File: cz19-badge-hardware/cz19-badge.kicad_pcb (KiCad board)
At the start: 4 copper layers, 391.4 x 293.4 mm, 323 parts, among them J1 USB_B_Micro, J3 Hook1, J4 Hook2, Q1 AO3400 (A09T), Q2 AO3400 (A09T), Q3 AO3400 (A09T), Q4 AO3400 (A09T), Q5 AO3400 (A09T), Q6 AO3400 (A09T), SW1 SW_Push, SW2 SW_Push, SW3 SW_Push, SW4 SW_Push, SW5 SW_Push, SW6 SW_Push, U1 SM16106, U10 XC6206P332PR, U11 ESP32-WROOM-32D, U2 SM16106, U3 SM16106, U4 SM16106, U5 SM16106, U6 SM16106, U7 TC7258E, U8 CH340C, U9 TP4056

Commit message: Finished PCB in 6mm pixel pitch (no SAO yet)
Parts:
- moved R14 308.0 mm to (25.0, -108.7)
- moved D257 304.0 mm to (38.1, -150.5)
- moved D258 304.0 mm to (40.6, -150.5)
- moved R10 304.0 mm to (42.1, -150.5)
- moved R9 304.0 mm to (36.6, -150.5)
- moved D260 294.1 mm to (42.1, -113.4)
- moved R13 294.1 mm to (43.6, -113.4)
- moved Q3 289.9 mm to (57.3, -112.1)
- moved R11 289.9 mm to (51.9, -112.1)
- moved R24 289.9 mm to (53.4, -112.1)
- moved D259 289.8 mm to (46.9, -113.4)
- moved R12 289.8 mm to (48.4, -113.4)
- moved R16 284.6 mm to (45.4, -135.1), turned to 270 degrees
- moved C1 283.5 mm to (73.8, -149.7)
- moved R15 282.9 mm to (72.3, -149.7)
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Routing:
- net GND: track 12.1 -> 295.6 mm, vias 0 -> 32
- net HUB75_OE: track 0.00 -> 261.4 mm, vias 0 -> 10
- net CLK: track 0.00 -> 248.5 mm, vias 0 -> 9
- net HUB75_LAT: track 0.00 -> 234.4 mm, vias 0 -> 9
- net G0: track 0.00 -> 180.1 mm, vias 0 -> 4
- net HUB75_R0: track 0.00 -> 179.5 mm, vias 0 -> 2
- net C: track 0.01 -> 179.2 mm, vias 0 -> 2
- net A: track 0.00 -> 170.7 mm
- net B: track 0.00 -> 170.6 mm
- net VUSB_SENSE: track 0.00 -> 167.6 mm, vias 0 -> 2
- net BTN_B: track 0.59 -> 166.1 mm, vias 0 -> 2
- net SCL: track 0.00 -> 159.7 mm
- net (no net): track 158.1 -> 0.00 mm, vias 32 -> 0
- net SDA: track 0.00 -> 154.7 mm
- net B0: track 0.00 -> 153.0 mm, vias 0 -> 2
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- added copper zone on 3V3.Cu, net 3V3
- added copper zone on B.Cu, net GND
- added copper zone on VCC.Cu, net VCC
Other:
- board size 391.4 x 293.4 mm -> 192 x 48 mm
- net class Power: trace_width 0.5 -> 0.3
- board text added: "CZ19 1337 badge proto v0.1 aka “Anakin”"
- board text removed: "CZ19 1337 badge proto v0.1 aka “Harry Potter”"
- board text removed: "Spoke width: 0.8mm"
- board text removed: "Spoke width: 1.2mm"

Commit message: Swapped left and right button
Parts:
- moved R23 232.1 mm to (184.3, 72.6), turned to 270 degrees
- moved R20 232.1 mm to (187.3, 72.6), turned to 270 degrees
- moved R21 230.4 mm to (185.8, 72.6), turned to 270 degrees
- moved SW4 228.4 mm to (75.3, 92.4)
- moved BT1 225.3 mm to (169.6, 106.1)
- moved C3 225.3 mm to (92.9, 102.2)
- moved C4 225.3 mm to (138.6, 90.0)
- moved D1 225.3 mm to (56.6, 72.3)
- moved D10 225.3 mm to (110.6, 72.3)
- moved D100 225.3 mm to (74.6, 90.3)
- moved D101 225.3 mm to (80.6, 90.3)
- moved D102 225.3 mm to (86.6, 90.3)
- moved D103 225.3 mm to (92.6, 90.3)
- moved D104 225.3 mm to (98.6, 90.3)
- moved D105 225.3 mm to (104.6, 90.3)
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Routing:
- net -BATT: track 38.4 -> 109.0 mm, vias 6 -> 0
- net Net-(Q4-Pad1): track 0.00 -> 24.4 mm
- net BTN_UP: track 36.1 -> 48.7 mm, vias 2 -> 4
- net BTN_RIGHT: track 51.4 -> 62.7 mm, vias 2 -> 4
- net 3V3: track 24.1 -> 33.9 mm, vias 6 -> 9
- net SCL: track 159.7 -> 167.2 mm, vias 0 -> 2
- net BTN_DOWN: track 60.5 -> 67.3 mm
- net SDA: track 154.7 -> 161.4 mm, vias 0 -> 2
- net G0: track 180.1 -> 186.4 mm, vias 4 -> 6
- net VCC: track 103.0 -> 106.2 mm
- net GND: track 295.6 -> 293.1 mm
- net B1: track 108.2 -> 110.0 mm, vias 2 -> 4
- net Net-(D33-Pad4): track 230.3 -> 231.6 mm
- net Net-(D65-Pad4): track 216.5 -> 217.3 mm
- net G1: track 106.6 -> 107.1 mm, vias 2 -> 4
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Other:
- net class Power: trace_width 0.3 -> 0.5
- board text added: "CZ19 1337 badge proto v0.2 aka “Forrest”"
- board text removed: "CZ19 1337 badge proto v0.1 aka “Anakin”"
- board text removed: "Spoke width: 0.508mm"

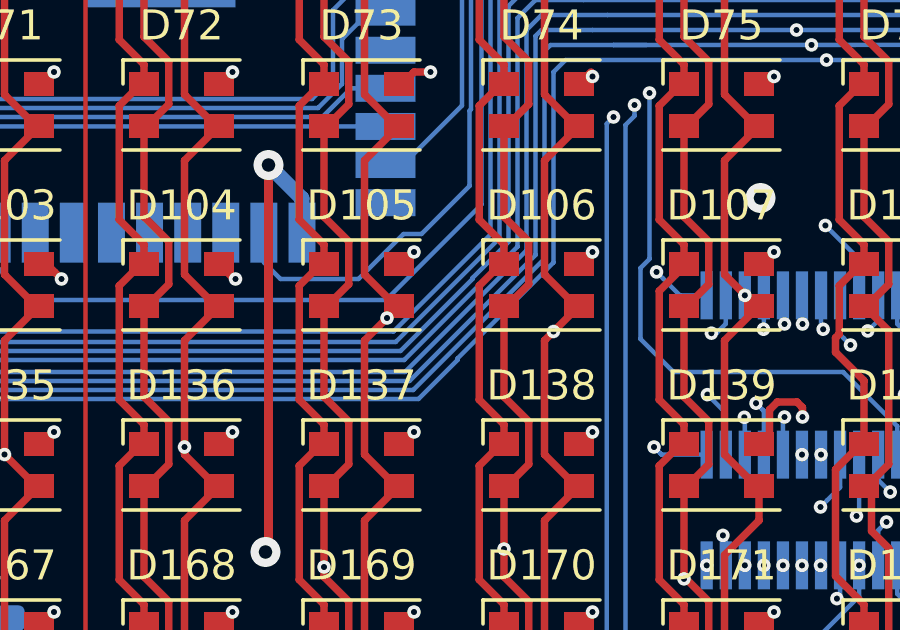
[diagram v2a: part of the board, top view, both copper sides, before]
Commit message: Added pulldown for GPIO12 to prevent boot instability due to flash voltage (seen through EMR)
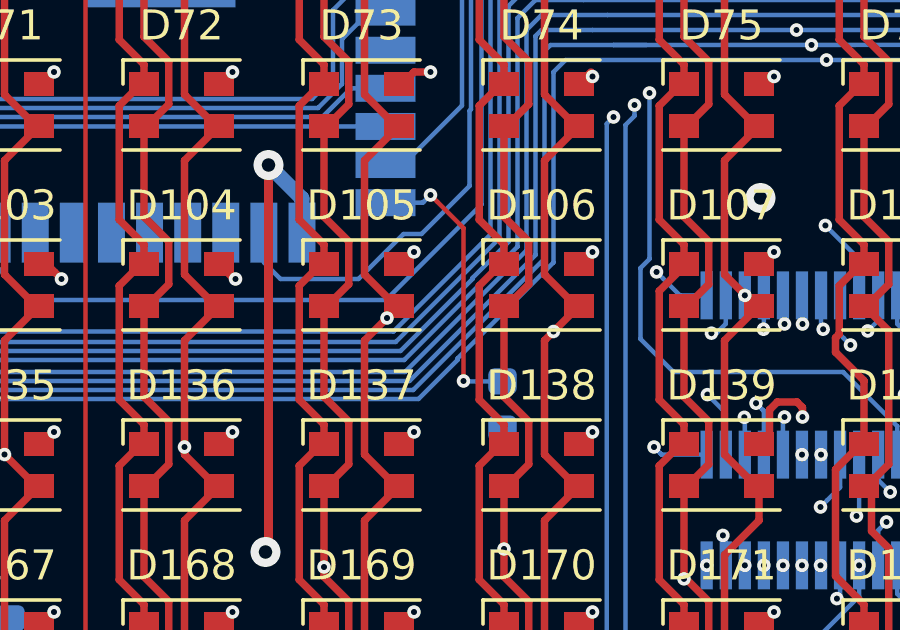
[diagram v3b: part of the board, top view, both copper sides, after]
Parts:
- added R33: 10k, Resistor_SMD:R_0603_1608Metric, B.Cu at (109.3, 94.3)
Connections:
- U11 pad 14: (no net) -> Net-(R33-Pad2)
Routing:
- net Net-(R33-Pad2): track 0.00 -> 9.57 mm, vias 0 -> 2

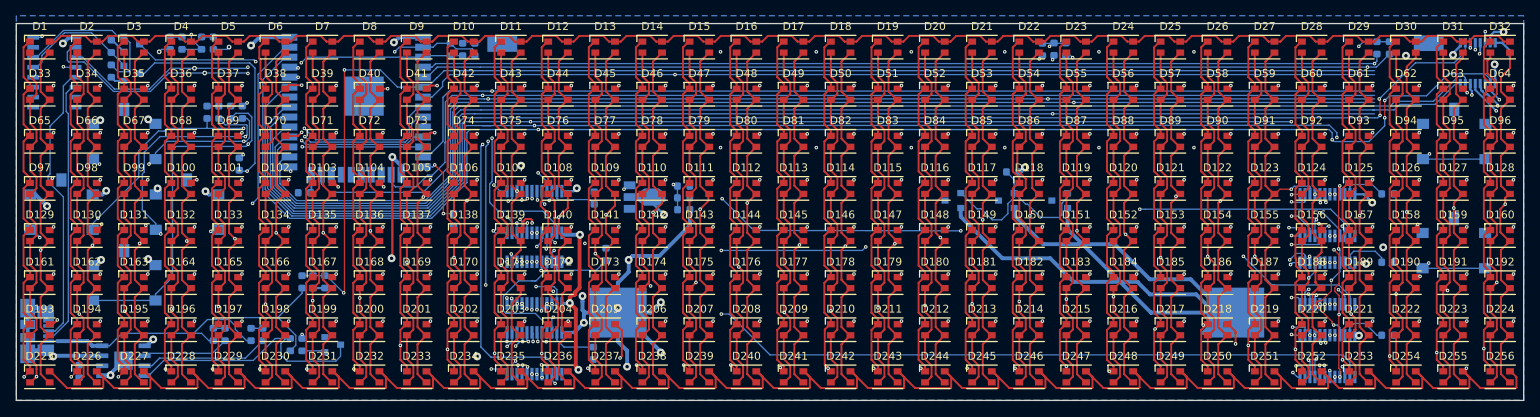
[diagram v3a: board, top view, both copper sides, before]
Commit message: Fixes: Footprint of row selector Space for vertical stacking Widen test point pads Reduce button distance Move vias away from pads
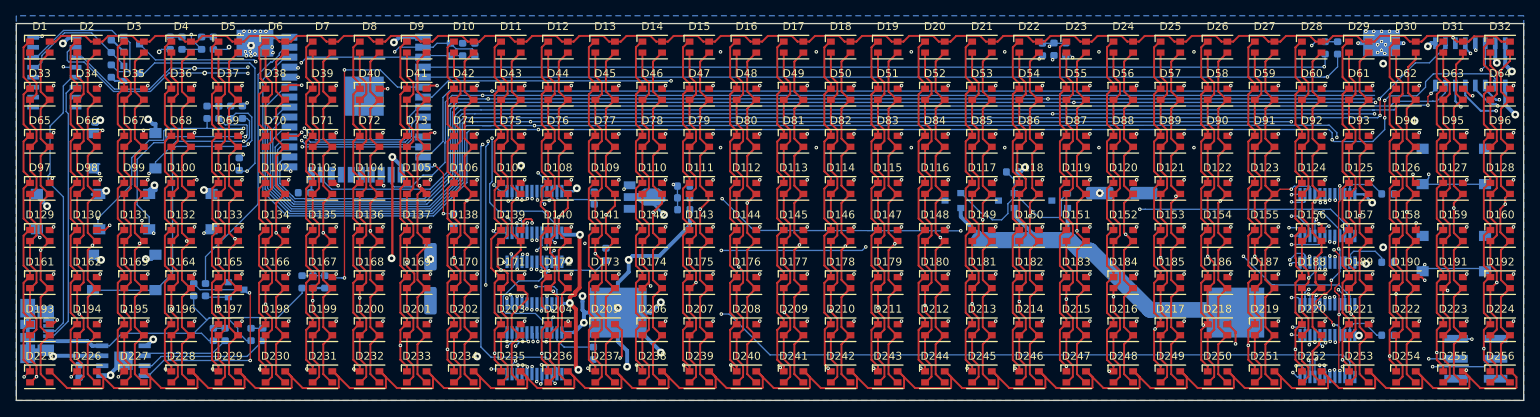
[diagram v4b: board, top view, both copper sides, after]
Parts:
- added C5: C, Capacitor_SMD:CP_Elec_6.3x5.4, B.Cu at (106.3, 101.8)
- added C6: C, Capacitor_SMD:CP_Elec_6.3x5.4, B.Cu at (194.4, 90.9)
- added J2: Conn_02x03_Counter_Clockwise, Connector_PinSocket_2.54mm:PinSocket_2x03_P2.54mm_Vertical_SMD, B.Cu at (239.5, 112.0)
- SW1, SW2, SW3, SW4, SW5, SW6: footprint Button_Switch_SMD:SW_SPST_B3S-1100 -> Button_Switch_SMD:SW_SPST_B3S-1000
- U7: footprint Package_SO:SSOP-16_3.9x4.9mm_P0.635mm -> Package_SO:SOIC-16_3.9x9.9mm_P1.27mm
- moved J3 31.5 mm to (84.0, 71.9)
- moved Q3 14.2 mm to (81.6, 103.2)
- moved R11 14.2 mm to (76.2, 103.2)
- moved R24 14.2 mm to (77.7, 103.2)
- moved R17 6.60 mm to (220.3, 72.4)
- moved R19 6.60 mm to (221.9, 72.4)
- moved J4 6.00 mm to (227.5, 71.8)
- moved SW5 4.10 mm to (236.7, 87.5)
- moved SW1 2.10 mm to (67.3, 85.5)
- moved SW6 1.30 mm to (236.7, 98.6)
- moved SW3 1.20 mm to (60.2, 93.2)
- moved SW4 1.20 mm to (74.5, 93.2)
- moved U7 0.96 mm to (238.8, 74.5)
- moved SW2 0.40 mm to (67.3, 101.0)
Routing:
- net VUSB_SENSE: track 167.6 -> 43.5 mm
- net VBAT_SENSE: track 140.4 -> 49.4 mm
- net SCL: track 167.2 -> 210.8 mm, vias 2 -> 4
- net SDA: track 161.4 -> 201.2 mm, vias 2 -> 4
- net -BATT: track 109.0 -> 83.2 mm
- net GND: track 293.1 -> 317.4 mm, vias 32 -> 59
- net Net-(R24-Pad2): track 44.7 -> 34.9 mm, vias 2 -> 0
- net VCC: track 106.2 -> 115.2 mm, vias 20 -> 23
- net BTN_B: track 166.1 -> 161.0 mm
- net A: track 170.7 -> 167.2 mm
- net C: track 179.3 -> 176.0 mm
- net B: track 170.6 -> 167.9 mm, vias 0 -> 2
- net Net-(Q3-Pad3): track 33.1 -> 30.5 mm, vias 0 -> 2
- net HUB75_OE: track 261.4 -> 263.7 mm
- net Net-(D108-Pad2): track 54.0 -> 56.0 mm
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
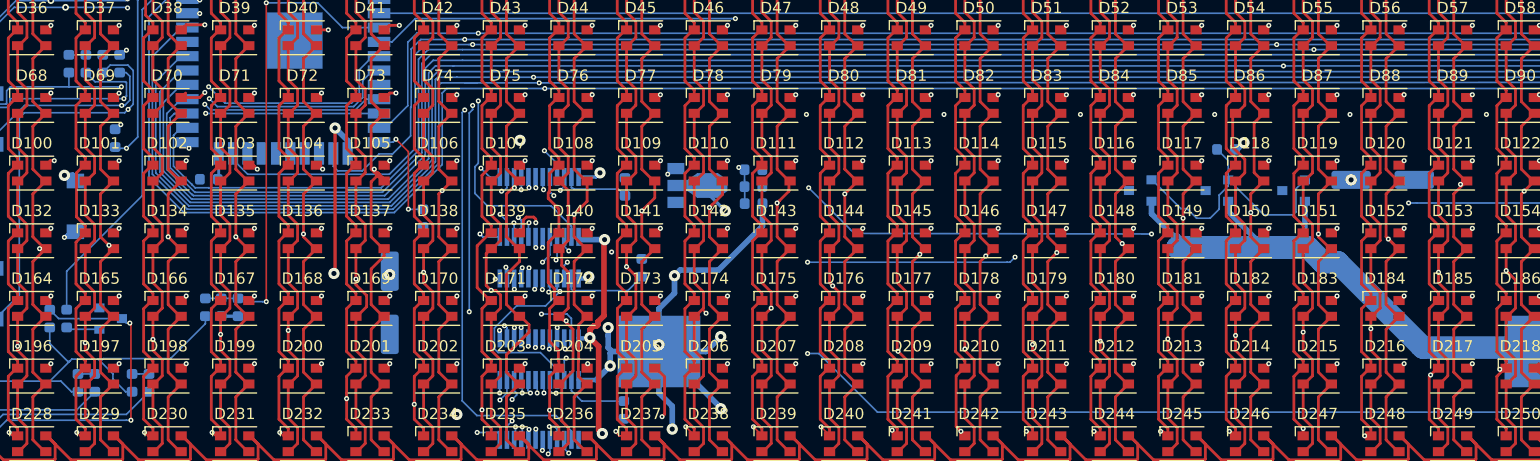
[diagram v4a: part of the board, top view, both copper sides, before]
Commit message: Fixes: Pulldown on charging_enable Add fiducials
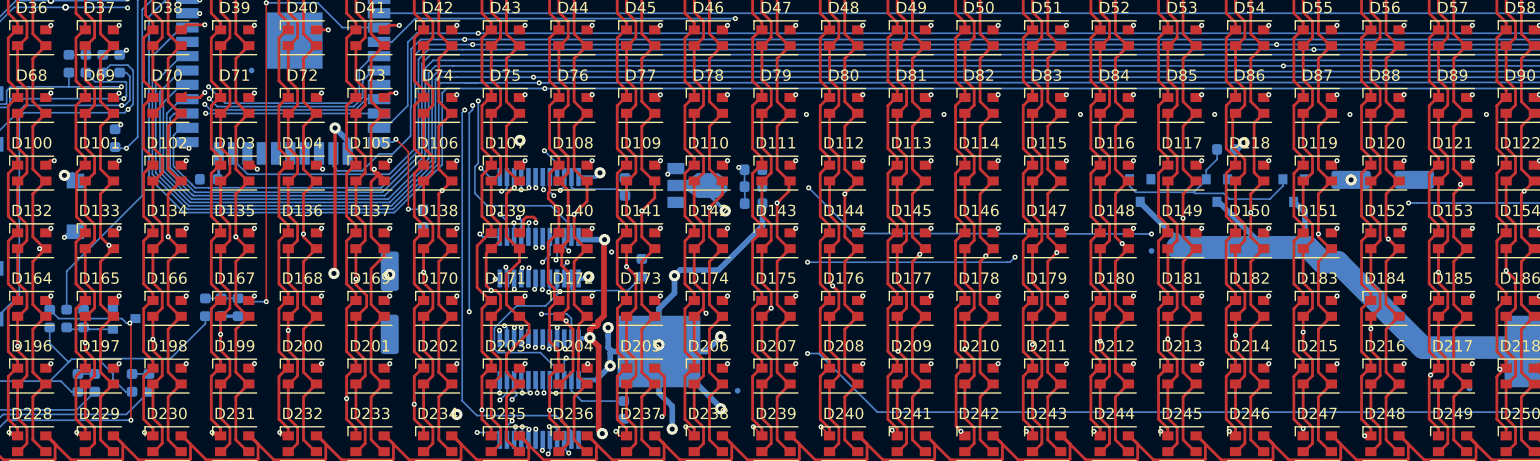
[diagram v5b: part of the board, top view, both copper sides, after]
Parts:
- added FID1: Fiducial, Fiducial:Fiducial_0.5mm_Mask1mm, B.Cu at (173.9, 97.2)
- added FID2: Fiducial, Fiducial:Fiducial_0.5mm_Mask1mm, B.Cu at (137.2, 109.6)
- added FID3: Fiducial, Fiducial:Fiducial_0.5mm_Mask1mm, B.Cu at (202.1, 109.4)
- added FID4: Fiducial, Fiducial:Fiducial_0.5mm_Mask1mm, B.Cu at (94.1, 81.2)
- added R34: 10k, Resistor_SMD:R_0603_1608Metric, B.Cu at (79.2, 103.2)
- D1, D10, D100, D101, D102, D103, D104, D105, D106, D107, D108, D109, D11, D110, D111, D112, D113, D114, D115, D116, D117, D118, D119, D12, D120, D121, D122, D123, D124, D125, D126, D127, D128, D129, D13, D130, D131, D132, D133, D134, D135, D136, D137, D138, D139, D14, D140, D141, D142, D143, D144, D145, D146, D147, D148, D149, D15, D150, D151, D152, D153, D154, D155, D156, D157, D158, D159, D16, D160, D161, D162, D163, D164, D165, D166, D167, D168, D169, D17, D170, D171, D172, D173, D174, D175, D176, D177, D178, D179, D18, D180, D181, D182, D183, D184, D185, D186, D187, D188, D189, D19, D190, D191, D192, D193, D194, D195, D196, D197, D198, D199, D2, D20, D200, D201, D202, D203, D204, D205, D206, D207, D208, D209, D21, D210, D211, D212, D213, D214, D215, D216, D217, D218, D219, D22, D220, D221, D222, D223, D224, D225, D226, D227, D228, D229, D23, D230, D231, D232, D233, D234, D235, D236, D237, D238, D239, D24, D240, D241, D242, D243, D244, D245, D246, D247, D248, D249, D25, D250, D251, D252, D253, D254, D255, D256, D26, D27, D28, D29, D3, D30, D31, D32, D33, D34, D35, D36, D37, D38, D39, D4, D40, D41, D42, D43, D44, D45, D46, D47, D48, D49, D5, D50, D51, D52, D53, D54, D55, D56, D57, D58, D59, D6, D60, D61, D62, D63, D64, D65, D66, D67, D68, D69, D7, D70, D71, D72, D73, D74, D75, D76, D77, D78, D79, D8, D80, D81, D82, D83, D84, D85, D86, D87, D88, D89, D9, D90, D91, D92, D93, D94, D95, D96, D97, D98, D99: value LED_RGBA -> LL-R3528RGBC-008-B
- D257: value YELLOW -> BLUE
- D258: value RED -> GREEN
- R10, R12, R13, R14, R9: value 1k -> 1k2
- U1, U2, U3, U4, U5, U6: value SM16106 -> SM16106SC
- moved Q3 1.20 mm to (82.8, 103.2)
- turned Q4 to 270 degrees
- turned Q5 to 270 degrees
- turned Q6 to 270 degrees
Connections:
- net CHARGE_ENABLE renamed ~CHARGE_ENABLE
- Q4 pad 2: -BATT -> GND
- Q4 pad 3: GND -> -BATT
- Q5 pad 2: -BATT -> GND
- Q5 pad 3: GND -> -BATT
- Q6 pad 2: -BATT -> GND
- Q6 pad 3: GND -> -BATT
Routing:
- net Net-(Q4-Pad1): track 24.4 -> 20.4 mm
- net ~CHARGE_ENABLE: track 2.97 -> 4.83 mm
- net -BATT: track 83.2 -> 84.4 mm
- net Net-(Q3-Pad3): track 30.5 -> 31.2 mm

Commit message: Preparing for production
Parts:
- added REF**: SOT-23-6, Package_TO_SOT_SMD:SOT-23-6, B.Cu at (166.9, 92.4)
- moved U7 90.9 mm to (149.3, 90.6)
- moved R23 69.5 mm to (114.8, 72.6)
- moved R21 69.5 mm to (116.3, 72.6)
- moved R20 69.5 mm to (117.8, 72.6)
- moved R5 5.60 mm to (232.0, 103.9)
- moved R6 5.24 mm to (223.7, 88.5)
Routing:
- net HUB75_R0: track 179.6 -> 66.0 mm
- net G0: track 186.0 -> 73.3 mm, vias 6 -> 5
- net B0: track 153.0 -> 40.6 mm
- net C: track 176.0 -> 87.3 mm
- net A: track 167.2 -> 90.0 mm, vias 0 -> 2
- net B: track 167.9 -> 91.1 mm
- net GND: track 317.4 -> 382.9 mm, vias 59 -> 58
- net Net-(D225-Pad4): track 353.4 -> 302.9 mm
- net VCC: track 115.2 -> 84.5 mm, vias 23 -> 21
- net Net-(D1-Pad4): track 205.4 -> 234.8 mm
- net 3V3: track 35.3 -> 64.0 mm
- net HUB75_OE: track 263.7 -> 247.6 mm
- net Net-(D33-Pad4): track 232.0 -> 243.0 mm
- net Net-(D129-Pad4): track 230.8 -> 221.3 mm, vias 33 -> 32
- net Net-(D100-Pad4): track 224.9 -> 217.5 mm, vias 33 -> 32
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
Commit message: Final gerbers
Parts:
- removed REF**: SOT-23-6, Package_TO_SOT_SMD:SOT-23-6
- added C7: 100nF, Capacitor_SMD:C_0603_1608Metric, B.Cu at (157.7, 89.8)
- added JP1: SolderJumper_2_Open, Jumper:SolderJumper-2_P1.3mm_Open_RoundedPad1.0x1.5mm, B.Cu at (176.4, 88.3)
- added JP2: SolderJumper_2_Open, Jumper:SolderJumper-2_P1.3mm_Bridged_RoundedPad1.0x1.5mm, B.Cu at (79.5, 86.5)
- added Q7: AO3400 (A09T), Package_TO_SOT_SMD:SOT-23, B.Cu at (172.2, 88.9)
- added Q8: AO3400 (A09T), Package_TO_SOT_SMD:SOT-23, B.Cu at (168.7, 93.2)
- added Q9: AO3400 (A09T), Package_TO_SOT_SMD:SOT-23, B.Cu at (172.2, 93.2)
- added R35: 470, Resistor_SMD:R_0603_1608Metric, B.Cu at (157.7, 88.1)
- added R36: 1k, Resistor_SMD:R_0603_1608Metric, B.Cu at (162.7, 93.3)
- added U12: DW-01, Package_TO_SOT_SMD:SOT-23-6, B.Cu at (157.5, 92.9)
- C5: value C -> 10uf; footprint Capacitor_SMD:CP_Elec_6.3x5.4 -> Capacitor_SMD:C_1206_3216Metric
- C6: value C -> 100uf; footprint Capacitor_SMD:CP_Elec_6.3x5.4 -> Capacitor_SMD:C_Elec_4x5.8
- R1, R2, R3, R4, R5, R6: value R -> 470
- moved Q6 18.0 mm to (168.7, 88.9), turned to 0 degrees
- moved Q4 12.3 mm to (185.2, 92.8), turned to 0 degrees
- moved C6 2.40 mm to (192.0, 90.9)
- moved Q5 1.53 mm to (180.9, 92.8), turned to 0 degrees
- moved C5 0.40 mm to (106.3, 101.4)
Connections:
- Q4 pad 2: GND -> GND_PROT
- Q5 pad 2: GND -> GND_PROT
- Q6 pad 1: Net-(Q4-Pad1) -> Net-(Q6-Pad1)
- Q6 pad 3: -BATT -> Net-(Q6-Pad3)
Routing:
- net GND_PROT: track 0.00 -> 34.0 mm, vias 0 -> 2
- net Net-(Q7-Pad1): track 0.00 -> 24.7 mm
- net -BATT: track 84.4 -> 65.9 mm
- net Net-(Q6-Pad1): track 0.00 -> 15.7 mm
- net GND: track 382.9 -> 391.3 mm
- net Net-(R36-Pad2): track 0.00 -> 5.15 mm
- net Net-(C7-Pad1): track 0.00 -> 3.94 mm
- net Net-(Q4-Pad1): track 20.4 -> 16.5 mm
- net VCC: track 84.5 -> 88.4 mm, vias 21 -> 22
- net ESP_FLASH: track 36.3 -> 38.7 mm
- net Net-(D100-Pad4): track 217.5 -> 219.3 mm
- net BTN_DOWN: track 66.0 -> 67.6 mm
- net Net-(Q8-Pad3): track 0.00 -> 1.50 mm
- net Net-(Q6-Pad3): track 0.00 -> 1.50 mm
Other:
- board text removed: "CHARGING"
- board text removed: "CZ19 1337 badge proto v0.2 aka “Forrest”"
- board text removed: "RX"
- board text removed: "STANDBY"
- board text removed: "TX"
